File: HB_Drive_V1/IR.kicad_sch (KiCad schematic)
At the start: 58 parts, among them J301 Conn_02x03_Odd_Even, J303 Conn_01x02, J304 Conn_02x04_Odd_Even, U301 TL082, U302 TL082, U303 TL082, U304 TL082, U305 TL082

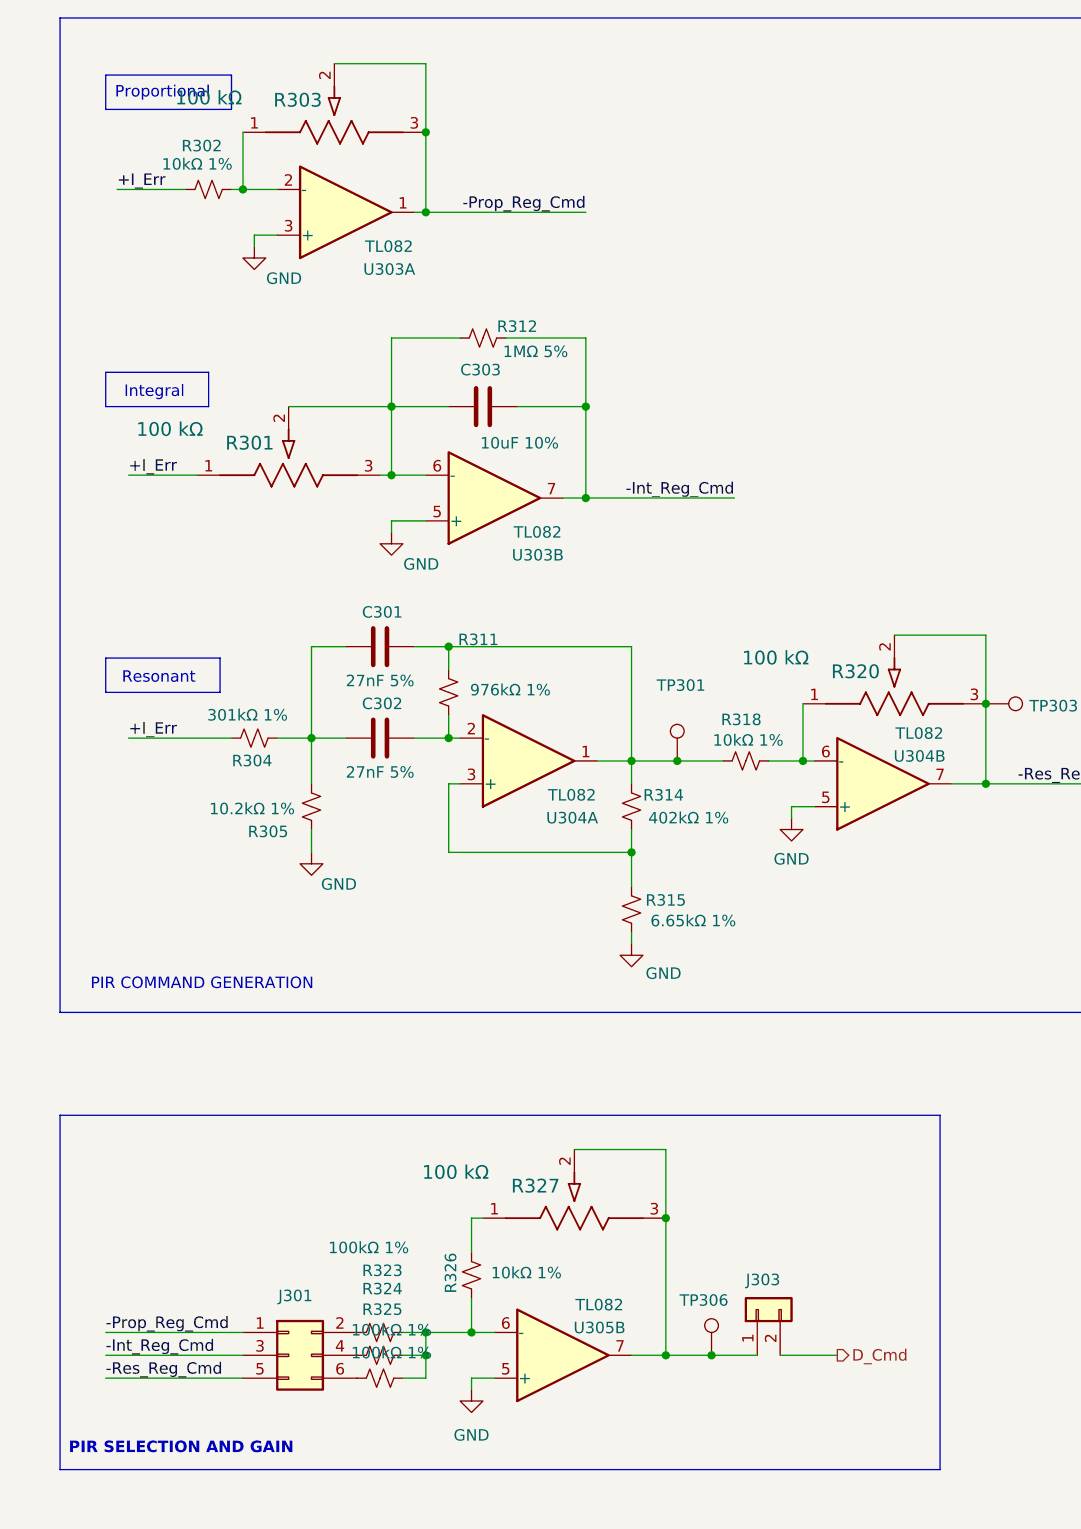
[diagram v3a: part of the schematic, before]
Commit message: Updates to 1st review corrected V2 of board
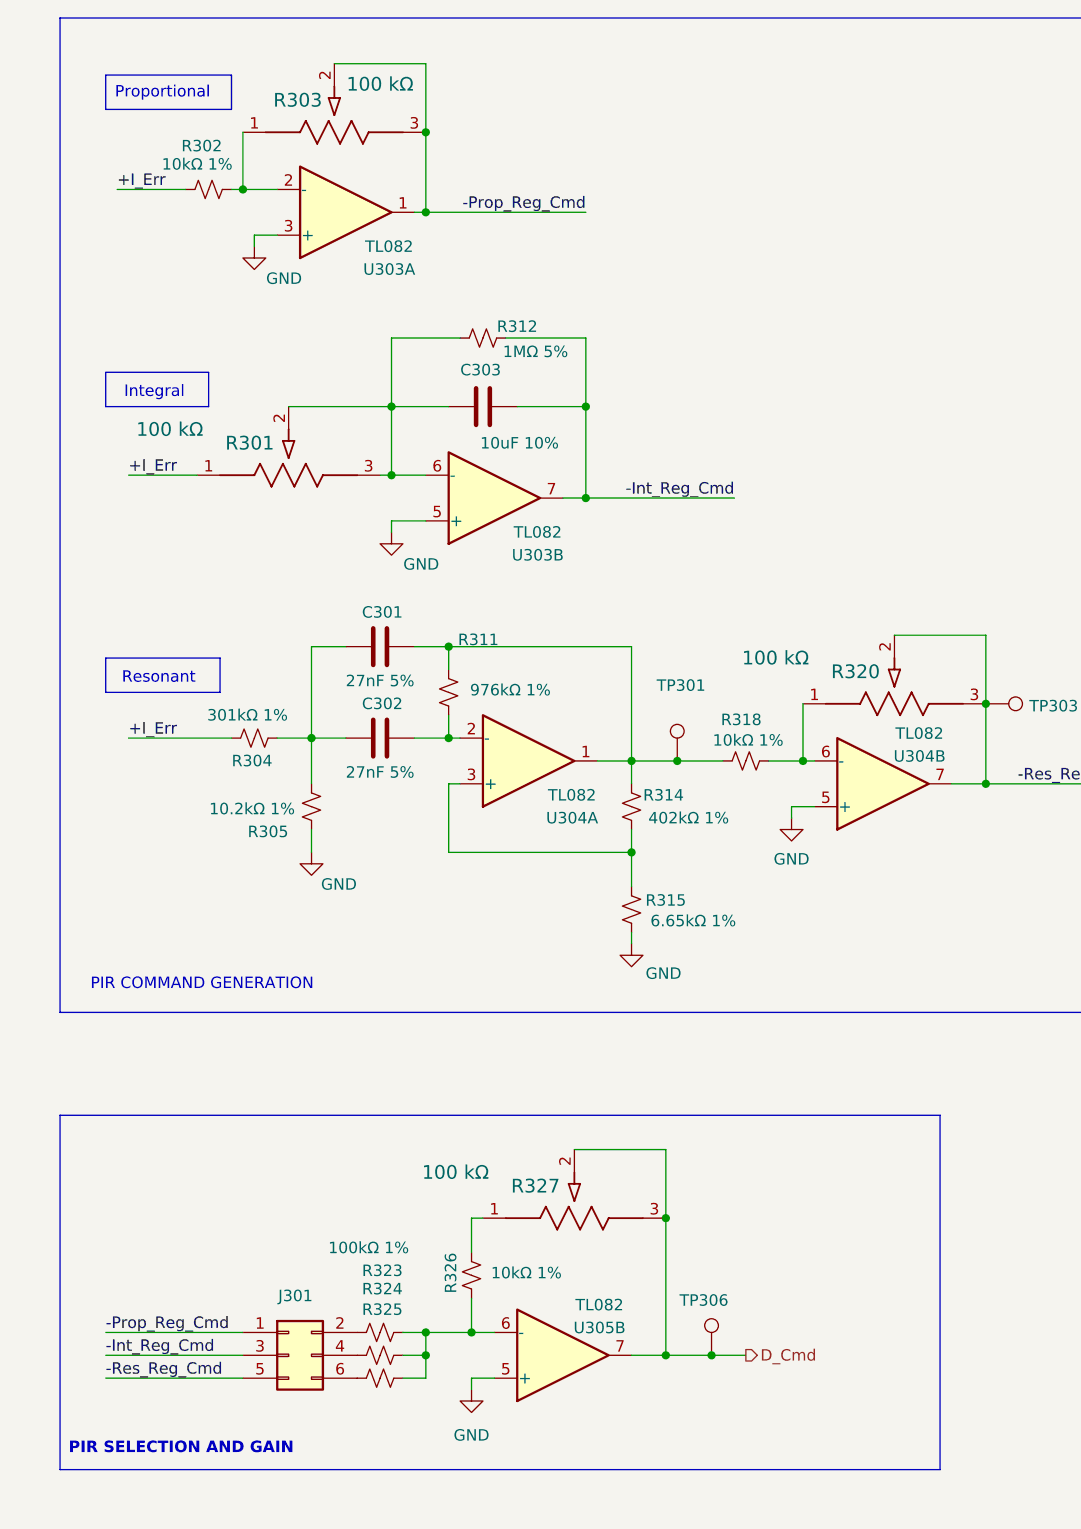
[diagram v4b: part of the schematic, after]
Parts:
- removed J303: Conn_01x02, Connector_PinHeader_2.54mm:PinHeader_1x02_P2.54mm_Vertical, symbol Connector_Generic:Conn_01x02
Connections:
- net D_Cmd: now also R327.2, R327.3, TP306.1, U305.7
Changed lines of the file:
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@@
 	)
 	(junction
-		(at 134.62 99.06)
+		(at 328.93 173.99)
 		(diameter 0)
 		(color 0 0 0 0)
 	)
 	(junction
-		(at 193.04 92.71)
+		(at 134.62 99.06)
 		(diameter 0)
 		(color 0 0 0 0)
 	)
 	(junction
-		(at 328.93 173.99)
+		(at 193.04 92.71)
 		(diameter 0)
 		(color 0 0 0 0)
@@
 	(wire
 		(pts
-			(xy 328.93 173.99) (xy 334.01 173.99)
+			(xy 328.93 173.99) (xy 332.74 173.99)
 		)
 		(stroke
@@
 	(wire
 		(pts
-			(xy 342.9 173.99) (xy 336.55 173.99)
-		)
-		(stroke
-			(width 0)
-			(type default)
-		)
-	)
-	(wire
-		(pts
 			(xy 113.03 99.06) (xy 109.22 99.06)
 		)
@@
 	(hierarchical_label "D_Cmd"
 		(shape output)
-		(at 342.9 173.99 0)
+		(at 332.74 173.99 0)
 		(effects
 			(font
@@
 		)
 		(property "Value" "100 kΩ"
-			(at 273.05 34.29 0)
+			(at 292.1 32.766 0)
 			(show_name no)
 			(do_not_autoplace no)
@@
 	)
 	(symbol
-		(lib_id "Connector_Generic:Conn_01x02")
-		(at 334.01 168.91 90)
-		(unit 1)
-		(body_style 1)
-		(exclude_from_sim no)
-		(in_bom yes)
-		(on_board yes)
-		(in_pos_files yes)
-		(dnp no)
-		(property "Reference" "J303"
-			(at 332.74 165.608 90)
-			(show_name no)
-			(do_not_autoplace no)
-			(effects
-				(font
-					(size 1.27 1.27)
-				)
-				(justify right)
-			)
-		)
-		(property "Value" "Conn_01x02"
-			(at 339.09 170.1799 90)
-			(hide yes)
-			(show_name no)
-			(do_not_autoplace no)
-			(effects
-				(font
-					(size 1.27 1.27)
-				)
-				(justify right)
-			)
-		)
-		(property "Footprint" "Connector_PinHeader_2.54mm:PinHeader_1x02_P2.54mm_Vertical"
-			(at 334.01 168.91 0)
-			(hide yes)
-			(show_name no)
-			(do_not_autoplace no)
-			(effects
-				(font
-					(size 1.27 1.27)
-				)
-			)
-		)
-		(property "Datasheet" ""
-			(at 334.01 168.91 0)
-			(hide yes)
-			(show_name no)
-			(do_not_autoplace no)
-			(effects
-				(font
-					(size 1.27 1.27)
-				)
-			)
-		)
-		(property "Description" "Generic connector, single row, 01x02, script generated (kicad-library-utils/schlib/autogen/connector/)"
-			(at 334.01 168.91 0)
-			(hide yes)
-			(show_name no)
-			(do_not_autoplace no)
-			(effects
-				(font
-					(size 1.27 1.27)
-				)
-			)
-		)
-		(property "Sim.Device" ""
-			(at 334.01 168.91 90)
-			(hide yes)
-			(show_name no)
-			(do_not_autoplace no)
-			(effects
-				(font
-					(size 1.27 1.27)
-				)
-			)
-		)
-		(pin "1"
-		)
-		(pin "2"
-		)
-		(instances
-			(project "HB_Drive_V1"
-				(path "/a9b54c89-4c8e-4c90-8a0d-ec2009e369b7/3e7f63a5-e260-45cd-8765-977a86943ed8"
-					(reference "J303")
-					(unit 1)
-				)
-			)
-		)
-	)
-	(symbol
 		(lib_id "Device:C")
 		(at 115.57 144.78 270)
@@
 		(property "Value" "100kΩ 1%"
 			(at 293.37 173.736 90)
+			(hide yes)
 			(show_name no)
 			(do_not_autoplace no)
@@
 		(property "Value" "100kΩ 1%"
 			(at 293.37 171.196 90)
+			(hide yes)
 			(show_name no)
 			(do_not_autoplace no)

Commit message: restores v2 to condtion as ordered!
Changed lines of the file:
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@@
 		(property "Value" "10kΩ 1%"
 			(at 129.794 101.6 90)
+			(hide yes)
 			(show_name no)
 			(do_not_autoplace no)
@@
 		(property "Value" "10kΩ 1%"
 			(at 129.794 96.52 90)
+			(hide yes)
 			(show_name no)
 			(do_not_autoplace no)
@@
 		(property "Value" "10kΩ 1%"
 			(at 129.794 99.06 90)
+			(hide yes)
 			(show_name no)
 			(do_not_autoplace no)

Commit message: Brings everything up to latest copy on my computer
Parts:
- added C314: 200pF 50V, Capacitor_SMD:C_0603_1608Metric, symbol Device:C
- added TP309, TP310: TestPoint, TestPoint:TestPoint_Loop_D2.60mm_Drill1.6mm_Beaded, symbol Connector:TestPoint
- R321: value 200 kΩ -> 500 kΩ
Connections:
- net -I_Fdbk: now also C314.1
- net -Int_Reg_Cmd: now also TP309.1
- net -Prop_Reg_Cmd: now also TP310.1
- net at R316.1, R317.1, R321.1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: now also C314.2
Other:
- company: (none) -> UW Madison, WEMPEC
- title: (none) -> HB Drive V3
- moved on the sheet: R321, TP305

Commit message: Makes annotation changes
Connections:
- net +I_Err: no longer R301.1, R302.1, R304.2
- net at R329.1, TP307.1, U305.1: now also R301.1, R302.1, R304.2
- net -Int_Reg_Cmd: no longer names the net of C303.1, J301.3 (Pin_3), R312.2, TP309.1, U303.7
- net -Prop_Reg_Cmd: no longer names the net of J301.1 (Pin_1), R303.2, R303.3, TP310.1, U303.1
- net -Res_Reg_Cmd: no longer names the net of J301.5 (Pin_5), R320.2, R320.3, TP303.1, U304.7
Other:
- moved on the sheet: C301, C302, C303, C304, C305, C306, C307, C308, C309, C310, C311, C312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
